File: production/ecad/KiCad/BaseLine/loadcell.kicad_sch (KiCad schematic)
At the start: 13 parts, among them J1 LoadCellConnector, U6 MIC920YC5-TR, U7 ADS1231IDR, U8 MIC920YC5-TR

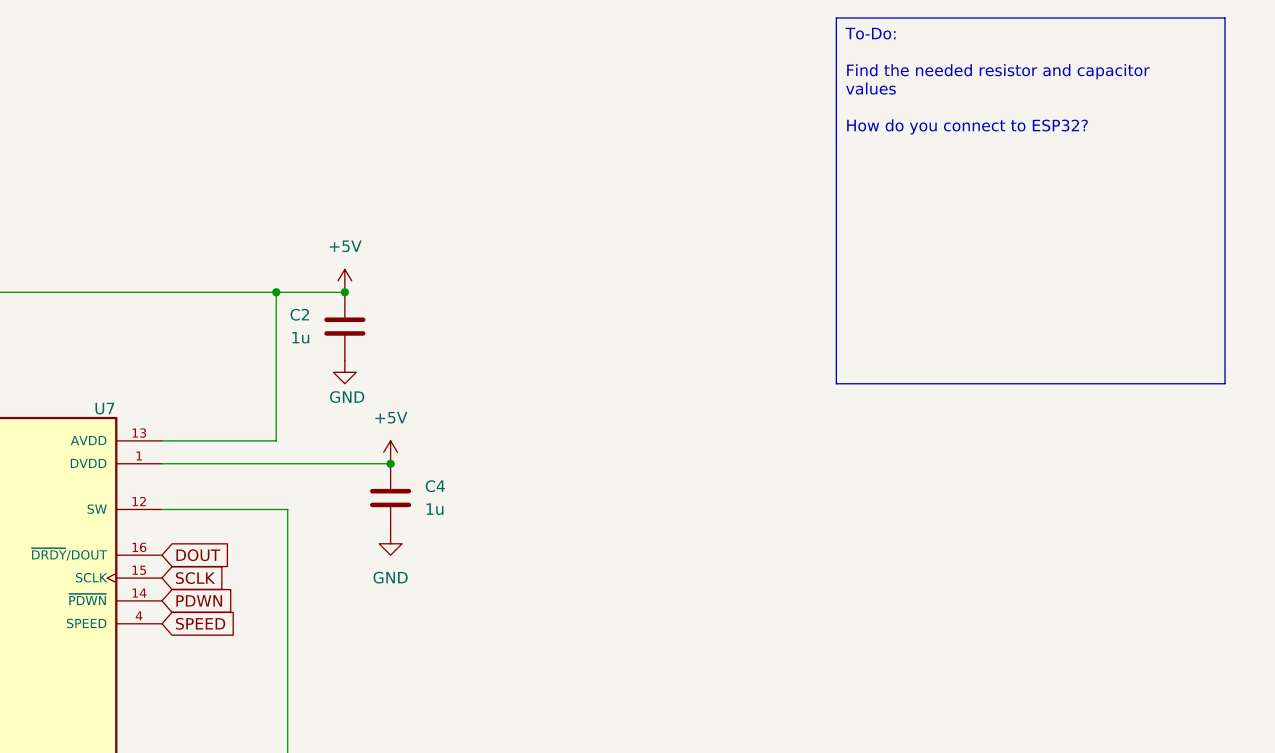
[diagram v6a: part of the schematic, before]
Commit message: MCU connections and matching names
matched the global net names of all the sensor connections with the MCU. Added an IO sheet for the power button
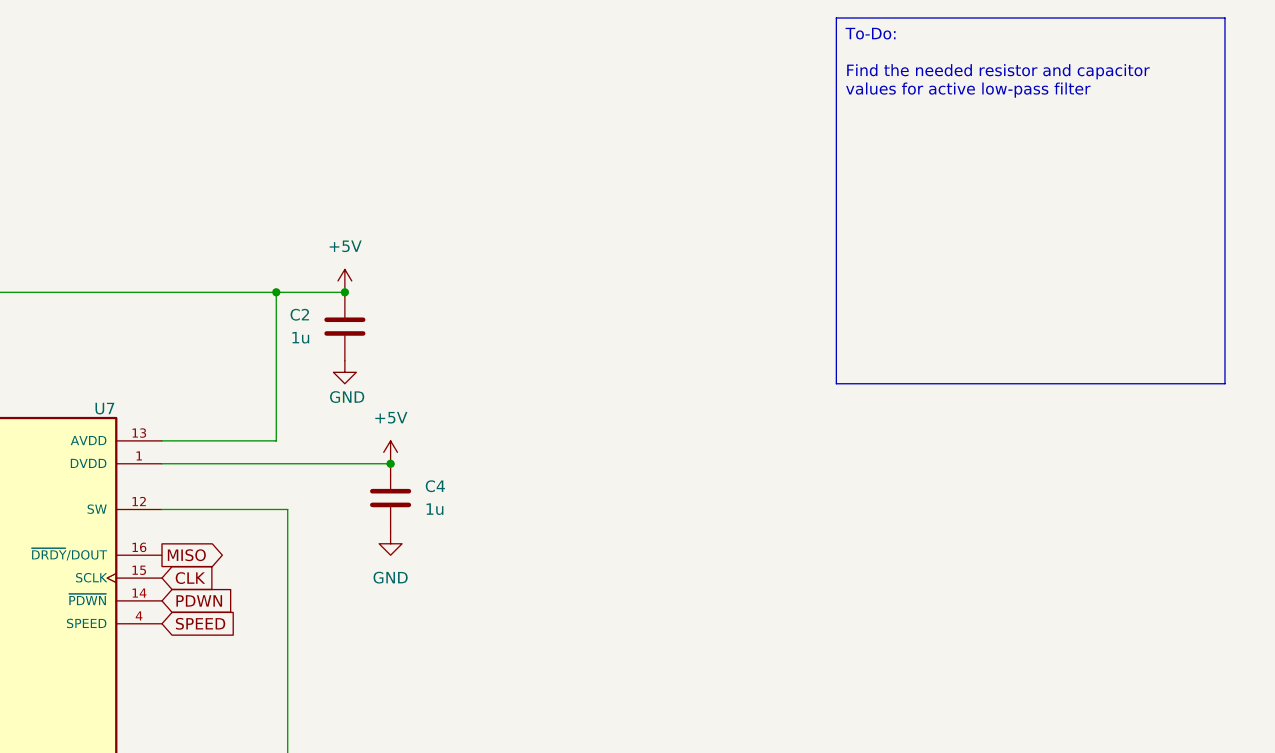
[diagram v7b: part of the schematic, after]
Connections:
- net DOUT renamed MISO
- net SCLK renamed CLK
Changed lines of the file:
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@@
 		)
 	)
-	(text_box "To-Do: \n\nFind the needed resistor and capacitor values\n\nHow do you connect to ESP32?\n"
+	(text_box "To-Do: \n\nFind the needed resistor and capacitor values for active low-pass filter\n\n"
 		(exclude_from_sim no)
 		(at 240.03 21.59 0)
@@
 		)
 	)
-	(global_label "DOUT"
-		(shape input)
+	(global_label "MISO"
+		(shape output)
 		(at 165.1 81.28 0)
 		(fields_autoplaced yes)
@@
 		)
 		(property "Intersheetrefs" "${INTERSHEET_REFS}"
-			(at 172.9838 81.28 0)
+			(at 172.6814 81.28 0)
 			(effects
 				(font
@@
 		)
 	)
-	(global_label "SCLK"
+	(global_label "CLK"
 		(shape input)
 		(at 165.1 83.82 0)
@@
 		)
 		(property "Intersheetrefs" "${INTERSHEET_REFS}"
-			(at 172.8628 83.82 0)
+			(at 171.6533 83.82 0)
 			(effects
 				(font

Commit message: Changed annotations
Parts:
- renumbered C16 to C18, C3 to C19, C2 to C20, C4 to C21, J1 to J4, R23 to R32, R25 to R33, R26 to R34, R24 to R35, U8 to U7, U7 to U8
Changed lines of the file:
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@@
 		(dnp no)
 		(fields_autoplaced yes)
-		(property "Reference" "#PWR064"
+		(property "Reference" "#PWR054"
 			(at 110.49 100.33 0)
 			(effects
@@
 			(project "BaseLine"
 				(path "/ba9eda21-3882-41e1-8265-3d8ac781da20/15451660-bad9-4e79-85d3-2d59df8c5ccd"
-					(reference "#PWR064")
+					(reference "#PWR054")
 					(unit 1)
 				)
@@
 		(on_board yes)
 		(dnp no)
-		(property "Reference" "#PWR051"
+		(property "Reference" "#PWR052"
 			(at 54.61 186.69 0)
 			(effects
@@
 			(project "BaseLine"
 				(path "/ba9eda21-3882-41e1-8265-3d8ac781da20/15451660-bad9-4e79-85d3-2d59df8c5ccd"
-					(reference "#PWR051")
+					(reference "#PWR052")
 					(unit 1)
 				)
@@
 		(on_board yes)
 		(dnp no)
-		(property "Reference" "J1"
+		(property "Reference" "J4"
 			(at 35.56 87.6299 0)
 			(effects
@@
 			(project "BaseLine"
 				(path "/ba9eda21-3882-41e1-8265-3d8ac781da20/15451660-bad9-4e79-85d3-2d59df8c5ccd"
-					(reference "J1")
+					(reference "J4")
 					(unit 1)
 				)
@@
 		(on_board yes)
 		(dnp no)
-		(property "Reference" "R26"
+		(property "Reference" "R34"
 			(at 50.546 175.514 90)
 			(effects
@@
 			(project "BaseLine"
 				(path "/ba9eda21-3882-41e1-8265-3d8ac781da20/15451660-bad9-4e79-85d3-2d59df8c5ccd"
-					(reference "R26")
+					(reference "R34")
 					(unit 1)
 				)
@@
 		(dnp no)
 		(fields_autoplaced yes)
-		(property "Reference" "R23"
+		(property "Reference" "R32"
 			(at 36.83 135.89 90)
 			(effects
@@
 			(project "BaseLine"
 				(path "/ba9eda21-3882-41e1-8265-3d8ac781da20/15451660-bad9-4e79-85d3-2d59df8c5ccd"
-					(reference "R23")
+					(reference "R32")
 					(unit 1)
 				)
@@
 		(on_board yes)
 		(dnp no)
-		(property "Reference" "U8"
+		(property "Reference" "U7"
 			(at 105.156 135.89 0)
 			(effects
@@
 			(project "BaseLine"
 				(path "/ba9eda21-3882-41e1-8265-3d8ac781da20/15451660-bad9-4e79-85d3-2d59df8c5ccd"
-					(reference "U8")
+					(reference "U7")
 					(unit 1)
 				)
@@
 		(dnp no)
 		(fields_autoplaced yes)
-		(property "Reference" "#PWR06"
+		(property "Reference" "#PWR060"
 			(at 190.5 74.93 0)
 			(effects
@@
 			(project "BaseLine"
 				(path "/ba9eda21-3882-41e1-8265-3d8ac781da20/15451660-bad9-4e79-85d3-2d59df8c5ccd"
-					(reference "#PWR06")
+					(reference "#PWR060")
 					(unit 1)
 				)
@@
 		(on_board yes)
 		(dnp no)
-		(property "Reference" "C2"
+		(property "Reference" "C20"
 			(at 181.61 54.6099 0)
 			(effects
@@
 			(project "BaseLine"
 				(path "/ba9eda21-3882-41e1-8265-3d8ac781da20/15451660-bad9-4e79-85d3-2d59df8c5ccd"
-					(reference "C2")
+					(reference "C20")
 					(unit 1)
 				)
@@
 		(dnp no)
 		(fields_autoplaced yes)
-		(property "Reference" "C16"
+		(property "Reference" "C18"
 			(at 80.01 124.46 90)
 			(effects
@@
 			(project "BaseLine"
 				(path "/ba9eda21-3882-41e1-8265-3d8ac781da20/15451660-bad9-4e79-85d3-2d59df8c5ccd"
-					(reference "C16")
+					(reference "C18")
 					(unit 1)
 				)
@@
 		(dnp no)
 		(fields_autoplaced yes)
-		(property "Reference" "#PWR050"
+		(property "Reference" "#PWR056"
 			(at 114.3 148.59 0)
 			(effects
@@
 			(project "BaseLine"
 				(path "/ba9eda21-3882-41e1-8265-3d8ac781da20/15451660-bad9-4e79-85d3-2d59df8c5ccd"
-					(reference "#PWR050")
+					(reference "#PWR056")
 					(unit 1)
 				)
@@
 		(dnp no)
 		(fields_autoplaced yes)
-		(property "Reference" "C4"
+		(property "Reference" "C21"
 			(at 194.31 73.6599 0)
 			(effects
@@
 			(project "BaseLine"
 				(path "/ba9eda21-3882-41e1-8265-3d8ac781da20/15451660-bad9-4e79-85d3-2d59df8c5ccd"
-					(reference "C4")
+					(reference "C21")
 					(unit 1)
 				)
@@
 		(dnp no)
 		(fields_autoplaced yes)
-		(property "Reference" "#PWR07"
+		(property "Reference" "#PWR061"
 			(at 190.5 85.09 0)
 			(effects
@@
 			(project "BaseLine"
 				(path "/ba9eda21-3882-41e1-8265-3d8ac781da20/15451660-bad9-4e79-85d3-2d59df8c5ccd"
-					(reference "#PWR07")
+					(reference "#PWR061")
 					(unit 1)
 				)
@@
 		(on_board yes)
 		(dnp no)
-		(property "Reference" "#PWR049"
+		(property "Reference" "#PWR053"
 			(at 55.88 151.13 0)
 			(effects
@@
 			(project "BaseLine"
 				(path "/ba9eda21-3882-41e1-8265-3d8ac781da20/15451660-bad9-4e79-85d3-2d59df8c5ccd"
-					(reference "#PWR049")
+					(reference "#PWR053")
 					(unit 1)
 				)
@@
 		(dnp no)
 		(fields_autoplaced yes)
-		(property "Reference" "R24"
+		(property "Reference" "R35"
 			(at 53.34 135.89 90)
 			(effects
@@
 			(project "BaseLine"
 				(path "/ba9eda21-3882-41e1-8265-3d8ac781da20/15451660-bad9-4e79-85d3-2d59df8c5ccd"
-					(reference "R24")
+					(reference "R35")
 					(unit 1)
 				)
@@
 		(on_board yes)
 		(dnp no)
-		(property "Reference" "C3"
+		(property "Reference" "C19"
 			(at 117.094 101.092 0)
 			(effects
@@
 			(project "BaseLine"
 				(path "/ba9eda21-3882-41e1-8265-3d8ac781da20/15451660-bad9-4e79-85d3-2d59df8c5ccd"
-					(reference "C3")
+					(reference "C19")
 					(unit 1)
 				)
@@
 		(dnp no)
 		(fields_autoplaced yes)
-		(property "Reference" "#PWR011"
+		(property "Reference" "#PWR057"
 			(at 165.1 115.57 0)
 			(effects
@@
 			(project "BaseLine"
 				(path "/ba9eda21-3882-41e1-8265-3d8ac781da20/15451660-bad9-4e79-85d3-2d59df8c5ccd"
-					(reference "#PWR011")
+					(reference "#PWR057")
 					(unit 1)
 				)
@@
 		(on_board yes)
 		(dnp no)
-		(property "Reference" "#PWR04"
+		(property "Reference" "#PWR059"
 			(at 185.42 66.04 0)
 			(effects
@@
 			(project "BaseLine"
 				(path "/ba9eda21-3882-41e1-8265-3d8ac781da20/15451660-bad9-4e79-85d3-2d59df8c5ccd"
-					(reference "#PWR04")
+					(reference "#PWR059")
 					(unit 1)
 				)
@@
 		(dnp no)
 		(fields_autoplaced yes)
-		(property "Reference" "#PWR052"
+		(property "Reference" "#PWR055"
 			(at 113.03 184.15 0)
 			(effects
@@
 			(project "BaseLine"
 				(path "/ba9eda21-3882-41e1-8265-3d8ac781da20/15451660-bad9-4e79-85d3-2d59df8c5ccd"
-					(reference "#PWR052")
+					(reference "#PWR055")
 					(unit 1)
 				)
@@
 		(on_board yes)
 		(dnp no)
-		(property "Reference" "#PWR09"
+		(property "Reference" "#PWR051"
 			(at 41.91 99.06 0)
 			(effects
@@
 			(project "BaseLine"
 				(path "/ba9eda21-3882-41e1-8265-3d8ac781da20/15451660-bad9-4e79-85d3-2d59df8c5ccd"
-					(reference "#PWR09")
+					(reference "#PWR051")
 					(unit 1)
 				)
@@
 		(on_board yes)
 		(dnp no)
-		(property "Reference" "R25"
+		(property "Reference" "R33"
 			(at 40.64 175.26 90)
 			(effects
@@
 			(project "BaseLine"
 				(path "/ba9eda21-3882-41e1-8265-3d8ac781da20/15451660-bad9-4e79-85d3-2d59df8c5ccd"
-					(reference "R25")
+					(reference "R33")
 					(unit 1)
 				)
@@
 		(on_board yes)
 		(dnp no)
-		(property "Reference" "#PWR05"
+		(property "Reference" "#PWR058"
 			(at 185.42 55.88 0)
 			(effects
@@
 			(project "BaseLine"
 				(path "/ba9eda21-3882-41e1-8265-3d8ac781da20/15451660-bad9-4e79-85d3-2d59df8c5ccd"
-					(reference "#PWR05")
+					(reference "#PWR058")
 					(unit 1)
 				)
@@
 		(on_board yes)
 		(dnp no)
-		(property "Reference" "U7"
+		(property "Reference" "U8"
 			(at 158.75 65.024 0)
 			(effects
@@
 			(project "BaseLine"
 				(path "/ba9eda21-3882-41e1-8265-3d8ac781da20/15451660-bad9-4e79-85d3-2d59df8c5ccd"
-					(reference "U7")
-					(unit 1)
-				)
+					(reference "U8")
+					(unit 1)
+				)
